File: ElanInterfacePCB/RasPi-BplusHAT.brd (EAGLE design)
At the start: 65 x 56 mm, 34 parts, among them K1 PIN20X2, Q1 310mA/60V/1.6Ω, Q10 1.1A/60V/600mΩ, Q11 310mA/60V/1.6Ω, Q12 1.1A/60V/600mΩ, Q2 1.1A/60V/600mΩ, Q3 310mA/60V/1.6Ω, Q4 1.1A/60V/600mΩ, Q5 310mA/60V/1.6Ω, Q6 1.1A/60V/600mΩ, Q7 310mA/60V/1.6Ω, Q8 1.1A/60V/600mΩ, Q9 310mA/60V/1.6Ω, U2 MAX481CUA+

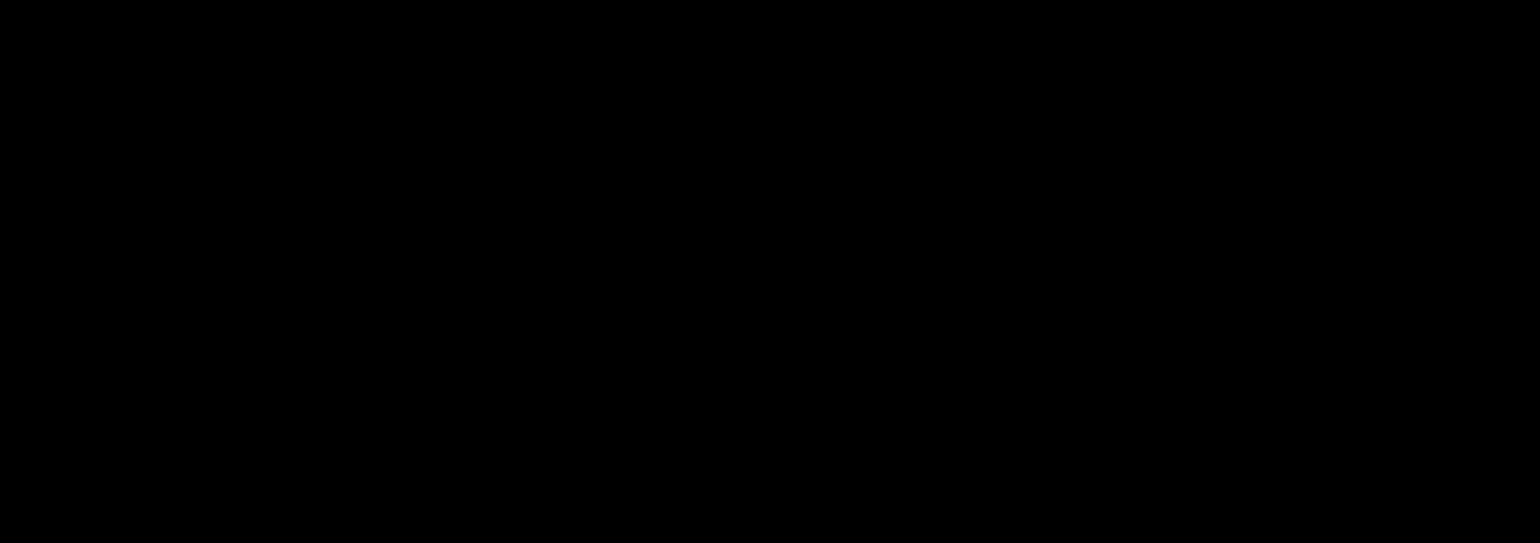
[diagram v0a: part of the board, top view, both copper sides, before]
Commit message: Fix pin numberbing on rj45
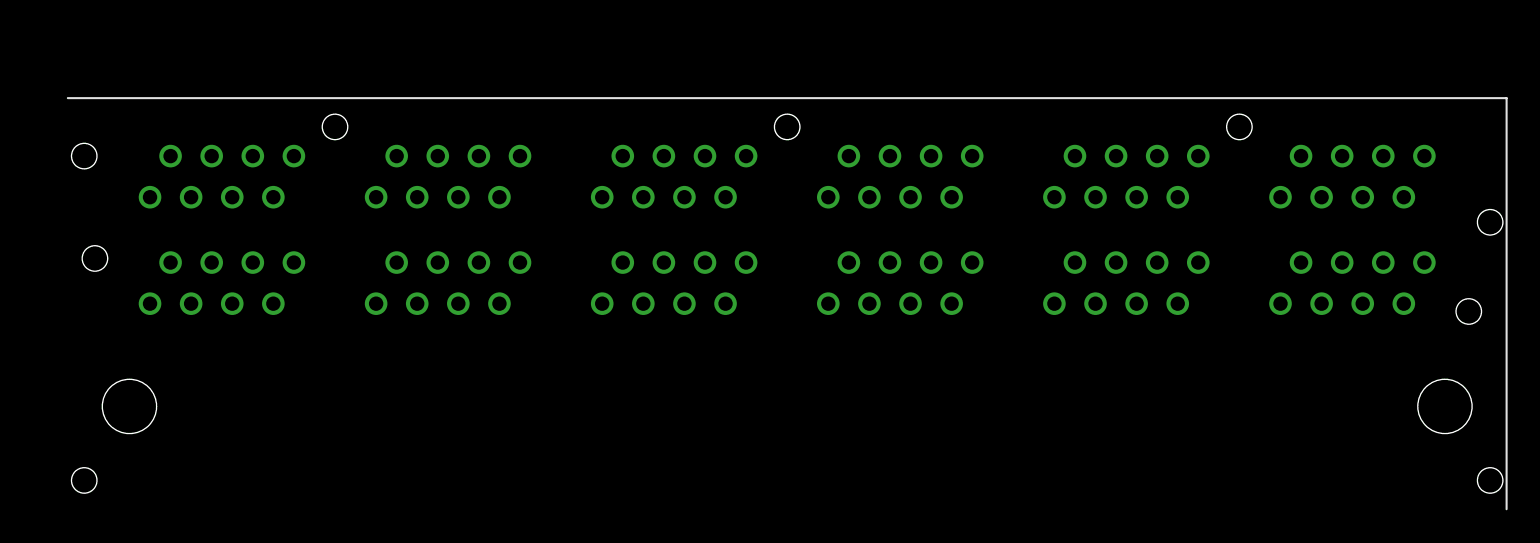
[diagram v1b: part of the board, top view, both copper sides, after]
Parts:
- added U$1: STEWARTSS73100, Stewart_Connector_SS73100-046F:STEWARTSS73100
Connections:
- new net N$13: U$1.P$16, U$1.P$8
- new net N$14: U$1.P$15, U$1.P$7
- new net N$15: U$1.P$14, U$1.P$6
- new net N$16: U$1.P$13, U$1.P$5
- new net N$17: U$1.P$12, U$1.P$4
- new net N$18: U$1.P$11, U$1.P$3
- new net N$19: U$1.P$10, U$1.P$2
- new net N$20: U$1.P$1, U$1.P$9
- new net N$21: U$1.P$17, U$1.P$25
- new net N$22: U$1.P$18, U$1.P$26
- new net N$23: U$1.P$19, U$1.P$27
- new net N$24: U$1.P$20, U$1.P$28
- new net N$25: U$1.P$21, U$1.P$29
- new net N$26: U$1.P$23, U$1.P$31
- new net N$27: U$1.P$22, U$1.P$30
- new net N$28: U$1.P$24, U$1.P$32
- new net N$29: U$1.P$33, U$1.P$41
- new net N$30: U$1.P$34, U$1.P$42
- new net N$31: U$1.P$35, U$1.P$43
- new net N$32: U$1.P$36, U$1.P$44
- new net N$33: U$1.P$37, U$1.P$45
- new net N$34: U$1.P$38, U$1.P$46
- new net N$35: U$1.P$39, U$1.P$47
- new net N$36: U$1.P$40, U$1.P$48
- new net N$37: U$1.P$49, U$1.P$57
- new net N$38: U$1.P$50, U$1.P$58
- new net N$39: U$1.P$51, U$1.P$59
- new net N$40: U$1.P$52, U$1.P$60
- new net N$41: U$1.P$53, U$1.P$61
- new net N$42: U$1.P$54, U$1.P$62
- new net N$43: U$1.P$55, U$1.P$63
- new net N$44: U$1.P$56, U$1.P$64
- new net N$45: U$1.P$65, U$1.P$73
- new net N$46: U$1.P$66, U$1.P$74
- new net N$47: U$1.P$67, U$1.P$75
- new net N$48: U$1.P$68, U$1.P$76
- new net N$49: U$1.P$69, U$1.P$77
- new net N$50: U$1.P$70, U$1.P$78
- new net N$51: U$1.P$71, U$1.P$79
- new net N$52: U$1.P$72, U$1.P$80
- new net N$53: U$1.P$81, U$1.P$89
- new net N$54: U$1.P$82, U$1.P$90
- new net N$55: U$1.P$83, U$1.P$91
- new net N$56: U$1.P$84, U$1.P$92
- new net N$57: U$1.P$85, U$1.P$93
- new net N$58: U$1.P$86, U$1.P$94
- new net N$59: U$1.P$87, U$1.P$95
- new net N$60: U$1.P$88, U$1.P$96

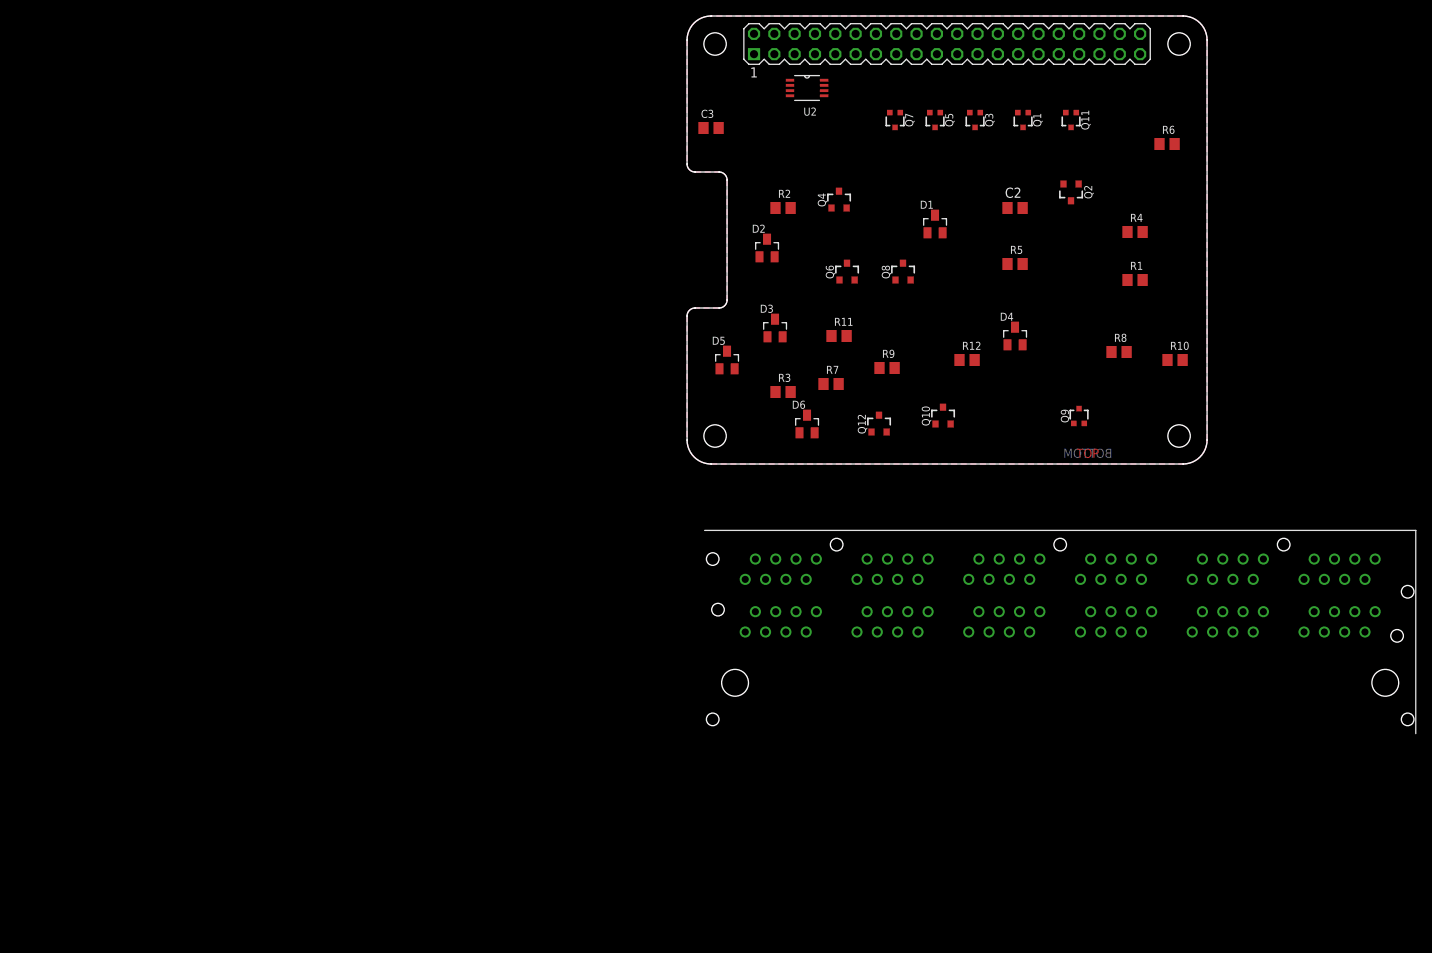
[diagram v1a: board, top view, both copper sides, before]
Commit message: Fixed pin inversion
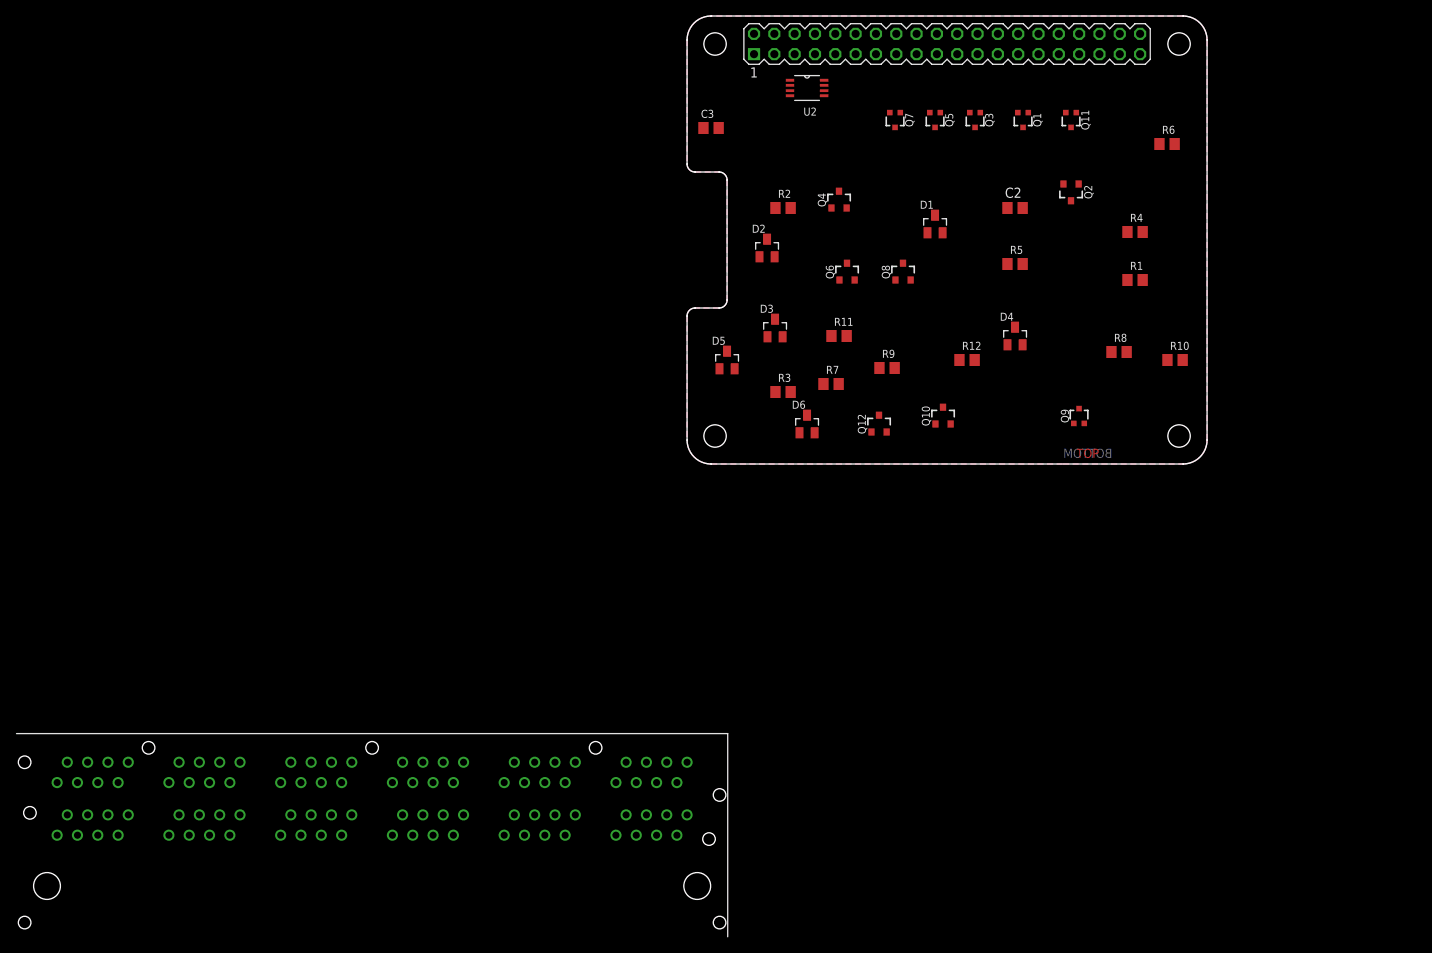
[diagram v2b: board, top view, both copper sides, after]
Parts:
- moved U$1 89.7 mm to (-80.0, -46.4)

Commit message: PCB Update
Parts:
- removed Q11: 310mA/60V/1.6Ω, SparkFun-DiscreteSemi:SOT323
- added C1, C4, C5, C6, C7: (no value), rcl:C0805
- added JP1: (no value), pinhead:2X04
- added Q13: 220mA/50V/3.5Ω, SparkFun-DiscreteSemi:SOT23-3
- Q1, Q3, Q5, Q7, Q9: value 310mA/60V/1.6Ω -> 220mA/50V/3.5Ω; device SparkFun-DiscreteSemi:SOT323 -> SparkFun-DiscreteSemi:SOT23-3
- moved U$1 111.0 mm to (4.32, 25.7)
- moved D6 81.0 mm to (86.6, 42.8)
- moved Q12 69.8 mm to (82.7, 42.8)
- moved R11 68.5 mm to (82.7, 41.0), flipped to the bottom
- moved Q9 48.1 mm to (78.8, 43.8), turned to 180 degrees
- moved R12 47.9 mm to (71.9, 43.5), turned to 180 degrees
- moved R8 47.0 mm to (17.0, 43.0), turned to 270 degrees
- moved D4 42.2 mm to (10.9, 45.6), turned to 180 degrees
- moved D5 40.8 mm to (27.3, 47.1), turned to 180 degrees
- moved R10 40.5 mm to (34.2, 43.5), turned to 270 degrees
- moved R6 37.7 mm to (22.4, 43.2), turned to 270 degrees
- moved Q10 37.5 mm to (31.6, 43.5), turned to 180 degrees
- moved R3 35.7 mm to (20.0, 43.8), flipped to the bottom, turned to 180 degrees
- moved D2 34.1 mm to (37.9, 46.6), turned to 180 degrees
- moved R2 34.0 mm to (44.3, 42.8), turned to 270 degrees
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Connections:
- removed net N$14: U$1.P$15, U$1.P$7
- removed net N$15 (its old number): U$1.P$14, U$1.P$6
- removed net N$16: U$1.P$13, U$1.P$5
- removed net N$17: U$1.P$12, U$1.P$4
- removed net N$19: U$1.P$10, U$1.P$2
- removed net N$22: U$1.P$18, U$1.P$26
- removed net N$26: U$1.P$23, U$1.P$31
- removed net N$27: U$1.P$22, U$1.P$30
- removed net N$30: U$1.P$34, U$1.P$42
- removed net N$34: U$1.P$38, U$1.P$46
- removed net N$35: U$1.P$39, U$1.P$47
- removed net N$38: U$1.P$50, U$1.P$58
- removed net N$42: U$1.P$54, U$1.P$62
- removed net N$43: U$1.P$55, U$1.P$63
- removed net N$46: U$1.P$66, U$1.P$74
- removed net N$50: U$1.P$70, U$1.P$78
- removed net N$51: U$1.P$71, U$1.P$79
- removed net N$54: U$1.P$82, U$1.P$90
- removed net N$58: U$1.P$86, U$1.P$94
- removed net N$59: U$1.P$87, U$1.P$95
- new net 485+: U$1.P$12, U$1.P$4, U2.8
- new net 485-: U$1.P$13, U$1.P$5, U2.1
- new net GPIO02: JP1.2, K1.3
- new net GPIO06: JP1.4, K1.31
- new net GPIO12: JP1.6, K1.32
- new net GPIO21: JP1.8, K1.40
- new net GPIOSEL: JP1.1, JP1.3, JP1.5, JP1.7, Q9.1
- new net ZONE2: R1.2, U$1.P$18, U$1.P$26
- new net ZONE3: R3.2, U$1.P$34, U$1.P$42
- new net ZONE4: R7.2, U$1.P$50, U$1.P$58
- new net ZONE5: R9.2, U$1.P$66, U$1.P$74
- new net ZONE6: R11.2, U$1.P$82, U$1.P$90
- net +12V: now also C1.1, C4.1, C5.1, C6.1, C7.1, U$1.P$14, U$1.P$22, U$1.P$30, U$1.P$38, U$1.P$46, U$1.P$54, U$1.P$6, U$1.P$62, U$1.P$70, U$1.P$78, U$1.P$86, U$1.P$94
- net +3V3: no longer K1.17
- net GND: now also C1.2, C4.2, C5.2, C6.2, C7.2, Q13.2, U$1.P$15, U$1.P$23, U$1.P$31, U$1.P$39, U$1.P$47, U$1.P$55, U$1.P$63, U$1.P$7, U$1.P$71, U$1.P$79, U$1.P$87, U$1.P$95; no longer Q11.2
- net GPIO07: now also Q13.1; no longer Q1.1, Q11.1
- net GPIO08: now also Q1.1; no longer Q3.1
- net GPIO09: now also Q3.1; no longer Q5.1
- net GPIO10: now also Q5.1; no longer Q7.1
- net GPIO11: now also Q7.1; no longer Q9.1
- net N$1: now also Q1.3; no longer Q3.3
- net N$11: now also Q9.3; no longer Q11.3
- net N$3: now also Q3.3; no longer Q5.3
- net N$4: now also Q13.3; no longer Q1.3
- net N$7: now also Q5.3; no longer Q7.3
- net N$9: now also Q7.3; no longer Q9.3
- net ZONE1: now also U$1.P$10, U$1.P$2; no longer R1.2, R11.2, R3.2, R7.2, R9.2
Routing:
- net +12V: track 0.00 -> 213.4 mm
- net GPIO02: track 0.00 -> 72.6 mm
- net GPIO12: track 0.00 -> 45.4 mm
- net GPIO06: track 0.00 -> 39.6 mm
- net GPIO21: track 0.00 -> 35.8 mm
- net 485-: track 0.00 -> 34.5 mm
- net 485+: track 0.00 -> 29.0 mm, vias 0 -> 1
- net N$55: track 0.00 -> 24.5 mm
- net N$47: track 0.00 -> 24.5 mm
- net N$39: track 0.00 -> 24.5 mm
- net N$31: track 0.00 -> 24.5 mm
- net N$23: track 0.00 -> 24.5 mm
- net N$15: track 0.00 -> 24.5 mm
- net ZONE4: track 0.00 -> 24.0 mm, vias 0 -> 1
- net RXI: track 0.00 -> 23.4 mm
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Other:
- board size 65 x 56 mm -> 90 x 56 mm
- board text added: "12"
- board text added: "2"
- board text added: "21"
- board text added: "6"

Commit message: Finished PCB
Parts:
- moved R4 5.91 mm to (50.4, 39.9), turned to 180 degrees
- moved R3 5.01 mm to (20.2, 38.8)
- moved R7 1.90 mm to (12.2, 39.8), flipped to the bottom
- moved R5 1.75 mm to (53.7, 43.1)
- moved Q13 1.50 mm to (50.5, 46.8)
- moved C5 1.25 mm to (57.0, 42.0)
- moved Q2 1.25 mm to (50.3, 43.0)
- moved R2 1.25 mm to (44.3, 41.5)
- moved C4 0.90 mm to (25.2, 42.8)
- moved D1 0.75 mm to (46.3, 46.7)
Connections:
- removed net +5V: K1.2, K1.4
- new net N$17: U2.6
- net ZONE1: now also R7.2; no longer R4.2
- net ZONE2: now also R3.2; no longer R1.2
- net ZONE3: now also R9.2; no longer R3.2
- net ZONE4: now also R1.2; no longer R7.2
- net ZONE5: now also R4.2; no longer R9.2
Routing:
- net GND: track 20.9 -> 391.1 mm, vias 5 -> 14
- net +12V: track 213.4 -> 308.0 mm, vias 0 -> 2
- net ZONE2: track 8.02 -> 22.9 mm, vias 0 -> 1
- net ZONE5: track 21.8 -> 36.6 mm
- net ZONE4: track 24.0 -> 37.8 mm
- net ZONE3: track 16.9 -> 29.5 mm, vias 0 -> 1
- net GPIO09: track 0.59 -> 13.0 mm
- net GPIO10: track 9.89 -> 20.1 mm
- net N$5: track 0.00 -> 10.1 mm, vias 0 -> 1
- net ZONE1: track 8.02 -> 18.0 mm, vias 0 -> 1
- net N$6: track 0.00 -> 9.93 mm, vias 0 -> 1
- net N$12: track 0.00 -> 8.05 mm, vias 0 -> 1
- net N$10: track 0.00 -> 5.96 mm, vias 0 -> 1
- net N$2: track 0.00 -> 5.91 mm, vias 0 -> 1
- net GPIO11: track 0.16 -> 5.25 mm
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
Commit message: Final v1 Board, as ordeded Minor PCB changes
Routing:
- net +12V: track 308.0 -> 307.1 mm
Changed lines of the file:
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@@
 <wire x1="85.375" y1="37.375" x2="86.5" y2="36.25" width="1.016" layer="1"/>
 <wire x1="86.5" y1="36.25" x2="86.5" y2="33.2166" width="1.016" layer="1"/>
-<wire x1="47.25" y1="35.648" x2="47.25" y2="36.5" width="1.016" layer="1"/>
 <wire x1="47.25" y1="36.5" x2="47.25" y2="38.75" width="1.016" layer="1"/>
 <wire x1="82.712" y1="43.858" x2="82.712" y2="38.788" width="0.3048" layer="1"/>

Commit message: Fixed inverted PMOS in schematic
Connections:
- net +12V: now also Q10.2, Q12.2, Q2.2, Q4.2, Q6.2, Q8.2; no longer Q10.3, Q12.3, Q2.3, Q4.3, Q6.3, Q8.3
- net N$10: now also Q10.3; no longer Q10.2
- net N$12: now also Q12.3; no longer Q12.2
- net N$2: now also Q4.3; no longer Q4.2
- net N$5: now also Q2.3; no longer Q2.2
- net N$6: now also Q6.3; no longer Q6.2
- net N$8: now also Q8.3; no longer Q8.2
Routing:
- net +12V: track 307.1 -> 277.8 mm
- net N$7: track 3.86 -> 0.08 mm
- net N$4: track 4.33 -> 1.89 mm
- net N$12: track 8.05 -> 5.69 mm
- net N$10: track 5.96 -> 4.16 mm
- net N$3: track 3.70 -> 2.02 mm
- net N$8: track 6.46 -> 4.89 mm
- net N$5: track 10.1 -> 8.59 mm
- net N$6: track 9.93 -> 8.67 mm
- net N$1: track 5.13 -> 4.06 mm
- net N$2: track 5.91 -> 4.99 mm
- net N$9: track 3.82 -> 3.03 mm
